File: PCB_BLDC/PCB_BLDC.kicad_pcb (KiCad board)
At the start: 2 copper layers, 152.4 x 119.4 mm, 70 parts, among them J1 Conn_01x01_Female, J10 Conn_01x06, J11 Conn_01x08, J12 Conn_01x06, J13 Conn_01x08, J14 Conn_01x08, J15 Conn_01x10, J16 Conn_01x08, J17 Conn_01x10, J2 Conn_01x01_Female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

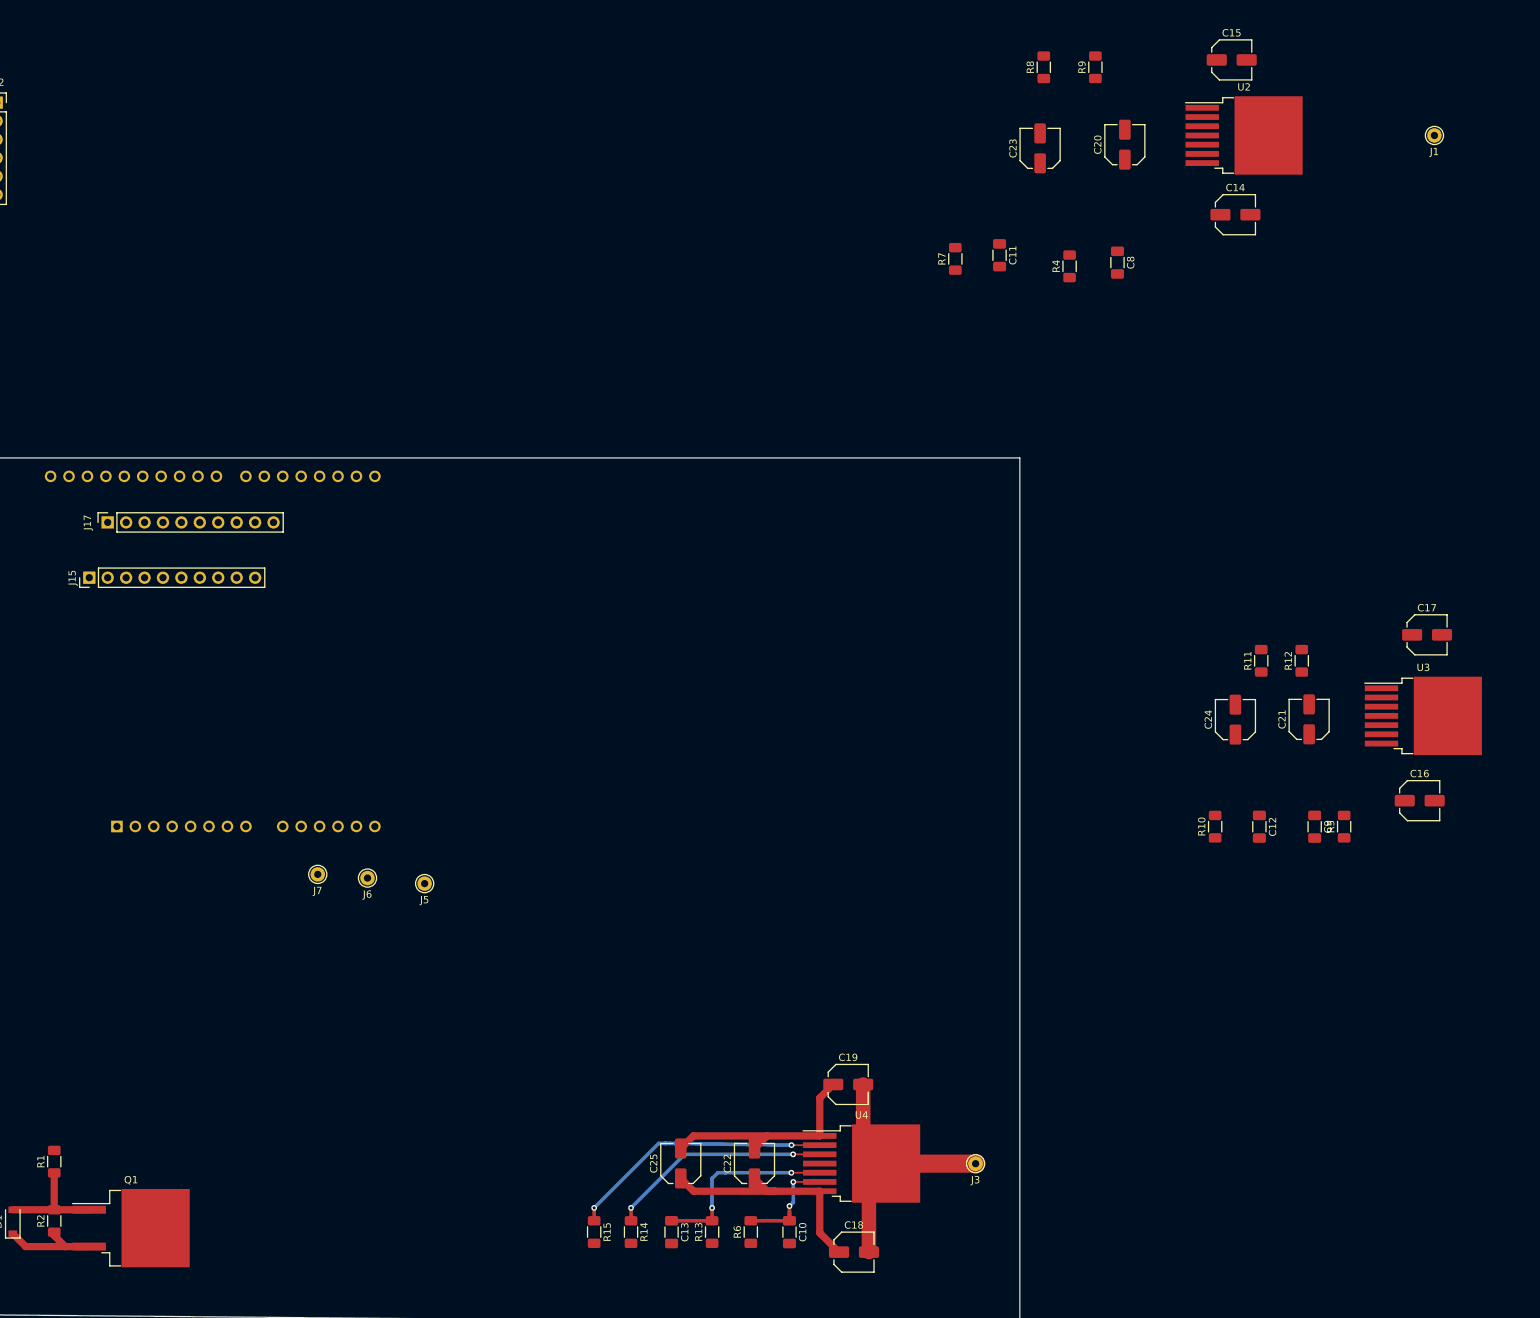
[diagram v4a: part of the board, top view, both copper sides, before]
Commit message: Main: Update Footprint, PCB Layout
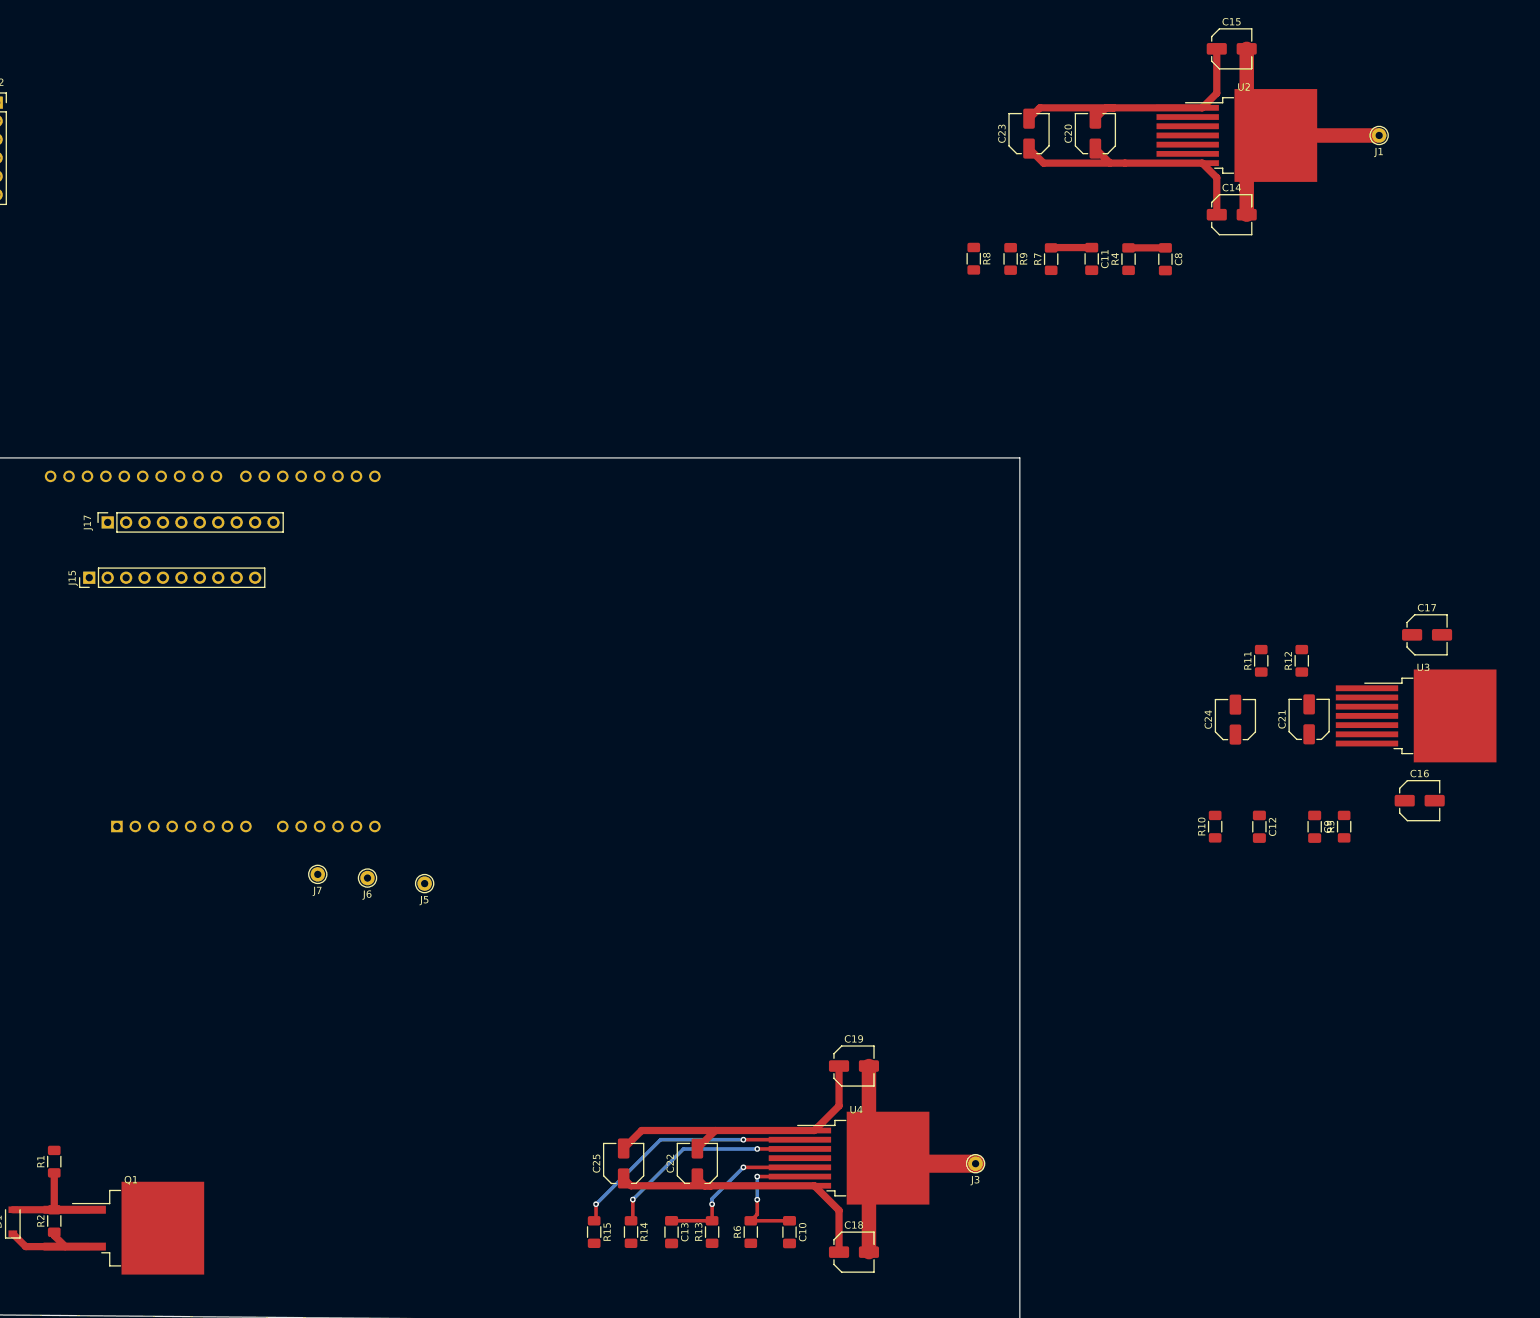
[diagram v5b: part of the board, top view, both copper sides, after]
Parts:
- R3: value 2k -> 100
- moved R9 28.9 mm to (208.3, -68.1), turned to 270 degrees
- moved R8 28.1 mm to (203.2, -68.1), turned to 270 degrees
- moved R7 13.2 mm to (213.9, -68.0)
- moved C11 12.7 mm to (219.5, -68.1)
- moved R4 8.19 mm to (224.5, -68.0)
- moved C22 7.87 mm to (165.1, 56.6)
- moved C25 7.87 mm to (154.9, 56.6)
- moved J1 7.62 mm to (259.1, -85.1)
- moved C8 6.62 mm to (229.6, -68.0)
- moved C20 4.34 mm to (220.0, -85.3)
- moved C19 2.66 mm to (186.7, 43.2)
- moved C23 2.54 mm to (210.8, -85.3)
- moved C15 1.52 mm to (238.8, -97.0)
- moved U4 1.05 mm to (187.0, 55.9)
- moved C14 0.51 mm to (238.8, -74.2)
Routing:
- net GND: track 34.7 -> 82.3 mm
- net /L1_Motor: track 0.00 -> 44.2 mm
- net /VCC_Filtered: track 32.9 -> 75.1 mm
- net /L3_Motor: track 37.7 -> 47.5 mm
- net Net-(C11-Pad1): track 0.00 -> 5.60 mm
- net /L1_IS: track 0.00 -> 5.08 mm
- net /L3_IS: track 15.1 -> 19.7 mm
- net Net-(C13-Pad1): track 27.4 -> 25.3 mm
- net Net-(R15-Pad1): track 36.8 -> 36.2 mm

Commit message: Main: Update Schmeatics, Add VCC
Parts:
- moved C5 216.4 mm to (168.0, 94.4)
- moved C3 172.1 mm to (145.8, 94.4)
- moved J5 149.3 mm to (201.9, 147.4)
- moved J6 149.3 mm to (194.1, 146.7)
- moved J7 149.3 mm to (187.2, 146.2)
- moved C20 143.6 mm to (210.1, 57.9)
- moved C23 143.6 mm to (201.2, 57.9)
- moved C14 143.3 mm to (228.9, 68.8)
- moved C15 143.3 mm to (228.9, 46.0)
- moved J1 143.3 mm to (249.2, 57.9)
- moved U2 143.3 mm to (230.6, 57.9)
- moved C2 138.8 mm to (131.2, 87.2)
- moved A1 136.8 mm to (95.6, 146.6)
- moved C8 120.8 mm to (195.5, 47.8), turned to 90 degrees
- moved L1 120.0 mm to (116.6, 80.5), turned to 0 degrees
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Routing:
- net /VCC_Filtered: track 75.1 -> 309.3 mm
- net /VCC_Polartiy_Check: track 13.5 -> 62.6 mm
- net GND: track 82.3 -> 127.6 mm
- net /L2_IS: track 0.00 -> 41.8 mm, vias 0 -> 2
- net /L2_Motor: track 0.00 -> 41.3 mm
- net /L1_IS: track 5.08 -> 40.4 mm, vias 0 -> 2
- net /VCC_Unregulated: track 0.00 -> 27.1 mm
- net Net-(C12-Pad1): track 0.00 -> 26.4 mm, vias 0 -> 2
- net Net-(C11-Pad1): track 5.60 -> 30.1 mm, vias 0 -> 2
- net /L3_IS: track 19.7 -> 44.1 mm
- net Net-(R15-Pad1): track 36.2 -> 16.5 mm
- net Net-(R9-Pad1): track 0.00 -> 17.5 mm, vias 0 -> 2
- net Net-(R8-Pad1): track 0.00 -> 16.8 mm, vias 0 -> 2
- net Net-(R11-Pad1): track 0.00 -> 16.8 mm, vias 0 -> 2
- net Net-(R12-Pad1): track 0.00 -> 16.5 mm, vias 0 -> 2
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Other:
- board size 152.4 x 119.4 mm -> 242.3 x 147.8 mm

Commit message: Main: Update Arduino Pins, PCB Routing
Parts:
- removed J10: Conn_01x06, Connector_PinHeader_2.54mm:PinHeader_1x06_P2.54mm_Vertical
- removed J11, J14: Conn_01x08, Connector_PinHeader_2.54mm:PinHeader_1x08_P2.54mm_Vertical
- removed J15: Conn_01x10, Connector_PinHeader_2.54mm:PinHeader_1x10_P2.54mm_Vertical
- moved J12 202.5 mm to (92.1, 111.5), turned to 90 degrees
- moved J13 202.0 mm to (69.2, 111.5), turned to 90 degrees
- moved J16 155.3 mm to (87.0, 63.2), turned to 90 degrees
- moved J17 137.3 mm to (60.1, 63.2)
- moved J5 107.6 mm to (188.2, 40.7), turned to 270 degrees
- moved U1 86.4 mm to (83.6, 90.7), turned to 0 degrees
- moved D3 84.3 mm to (68.7, 94.8)
- moved R3 84.3 mm to (75.0, 94.8)
- moved D2 82.3 mm to (103.8, 85.5)
- moved R6 74.9 mm to (135.9, 90.0), turned to 180 degrees
- moved C19 74.8 mm to (166.9, 86.2)
- moved C22 74.8 mm to (145.3, 99.6)
- moved C25 74.8 mm to (135.2, 99.6)
- moved J3 74.8 mm to (183.9, 99.9)
- moved C18 74.8 mm to (166.9, 111.8)
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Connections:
- A1 pad 12: Net-(A1-Pad12) -> /A3
- A1 pad 13: Net-(A1-Pad13) -> /A4
- A1 pad 14: Net-(A1-Pad14) -> /A5
- A1 pad 15: Net-(A1-Pad15) -> /D0
- A1 pad 16: Net-(A1-Pad16) -> /D1
- A1 pad 17: /L1_IN -> /D2
- A1 pad 18: /L2_IN -> /D3
- A1 pad 19: /L3_IN -> /D4
- A1 pad 2: Net-(A1-Pad2) -> /IOREF
- A1 pad 20: /L1_INH -> /D5
- A1 pad 21: /L2_INH -> /D6
- A1 pad 22: /L3_INH -> /D7
- A1 pad 23: /L1_IS -> /D8
- A1 pad 24: /L2_IS -> /D9
- A1 pad 25: /L3_IS -> /D10
- A1 pad 26: Net-(A1-Pad26) -> /D11
- A1 pad 3: Net-(A1-Pad3) -> /Reset
- A1 pad 30: Net-(A1-Pad30) -> /AREF
- A1 pad 31: Net-(A1-Pad31) -> /SDA
- A1 pad 32: Net-(A1-Pad32) -> /SCL
- A1 pad 4: Net-(A1-Pad4) -> /3V3
- A1 pad 5: Net-(A1-Pad5) -> /5V
- C10 pad 1: /L3_IS -> /D3
- C8 pad 1: /L1_IS -> /D7
- C9 pad 1: /L2_IS -> /D5
- J12 pad 1: Net-(J12-Pad1) -> /L1_Sense
- J12 pad 2: Net-(J12-Pad2) -> /L2_Sense
- J12 pad 3: Net-(J12-Pad3) -> /L3_Sense
- J12 pad 4: Net-(J12-Pad4) -> /A3
- J12 pad 5: Net-(J12-Pad5) -> /A4
- J12 pad 6: Net-(J12-Pad6) -> /A5
- J13 pad 2: Net-(J13-Pad2) -> /IOREF
- J13 pad 3: Net-(J13-Pad3) -> /Reset
- J13 pad 4: Net-(J13-Pad4) -> /3V3
- J13 pad 5: Net-(J13-Pad5) -> /5V
- J13 pad 6: Net-(J13-Pad6) -> GND
- J13 pad 7: Net-(J13-Pad7) -> GND
- J13 pad 8: Net-(J13-Pad8) -> /VCC_5V
- J16 pad 1: Net-(J16-Pad1) -> /D7
- J16 pad 2: Net-(J16-Pad2) -> /D6
- J16 pad 3: Net-(J16-Pad3) -> /D5
- J16 pad 4: Net-(J16-Pad4) -> /D4
- J16 pad 5: Net-(J16-Pad5) -> /D3
- J16 pad 6: Net-(J16-Pad6) -> /D2
- J16 pad 7: Net-(J16-Pad7) -> /D1
- J16 pad 8: Net-(J16-Pad8) -> /D0
- J17 pad 1: Net-(J17-Pad1) -> /SCL
- J17 pad 10: Net-(J17-Pad10) -> /D8
- J17 pad 2: Net-(J17-Pad2) -> /SDA
- J17 pad 3: Net-(J17-Pad3) -> /AREF
- J17 pad 4: Net-(J17-Pad4) -> GND
- J17 pad 5: Net-(J17-Pad5) -> /Rot_A_Pull_Up
- J17 pad 6: Net-(J17-Pad6) -> /Rot_B_Pull_Up
- J17 pad 7: Net-(J17-Pad7) -> /D11
- J17 pad 8: Net-(J17-Pad8) -> /D10
- J17 pad 9: Net-(J17-Pad9) -> /D9
- R11 pad 2: /L2_INH -> /D6
- R12 pad 2: /L2_IN -> /D10
- R14 pad 2: /L3_INH -> /D4
- R15 pad 2: /L3_IN -> /D9
- R4 pad 2: /L1_IS -> /D7
- R5 pad 2: /L2_IS -> /D5
- R6 pad 2: /L3_IS -> /D3
- R8 pad 2: /L1_INH -> /D8
- R9 pad 2: /L1_IN -> /D11
- U2 pad 6: /L1_IS -> /D7
- U3 pad 6: /L2_IS -> /D5
- U4 pad 6: /L3_IS -> /D3
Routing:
- net /D11: track 0.00 -> 126.4 mm
- net /D7: track 0.00 -> 118.7 mm, vias 0 -> 2
- net /D3: track 0.00 -> 116.6 mm, vias 0 -> 4
- net /D8: track 0.00 -> 112.8 mm
- net /D10: track 0.00 -> 112.8 mm, vias 0 -> 2
- net /D9: track 0.00 -> 104.6 mm, vias 0 -> 2
- net /D5: track 0.00 -> 101.4 mm, vias 0 -> 4
- net /D4: track 0.00 -> 100.6 mm, vias 0 -> 2
- net /D6: track 0.00 -> 81.8 mm, vias 0 -> 2
- net /L3_IS: track 44.1 -> 0.00 mm, vias 2 -> 0
- net /L2_IS: track 41.8 -> 0.00 mm, vias 2 -> 0
- net /L1_IS: track 40.4 -> 0.00 mm, vias 2 -> 0
- net /VCC_5V: track 15.5 -> 55.2 mm
- net /Rot_B_Pull_Up: track 7.73 -> 37.8 mm
- net /L1_Sense: track 0.00 -> 26.6 mm
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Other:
- board size 242.3 x 147.8 mm -> 268.2 x 169.3 mm

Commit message: Main: Update Routing, Schmematic to use Analog Ports of Arduino
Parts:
- removed J1, J2, J3, J4, J5, J6, J7: Conn_01x01_Female, Connector_Pin:Pin_D1.0mm_L10.0mm
- added J10: Conn_01x06, Connector_PinSocket_2.54mm:PinSocket_1x06_P2.54mm_Vertical, F.Cu at (97.4, 107.8)
- added J11: Conn_01x07, TerminalBlock_Phoenix:TerminalBlock_Phoenix_MKDS-1,5-7_1x07_P5.00mm_Horizontal, F.Cu at (201.9, 95.7)
- moved D2 40.5 mm to (108.5, 125.7)
- moved U1 37.7 mm to (97.5, 125.7), turned to 180 degrees
- moved D3 32.4 mm to (78.9, 125.5)
- moved R3 32.4 mm to (85.2, 125.5)
- moved J9 21.7 mm to (31.5, 123.2)
- moved J8 20.0 mm to (32.0, 143.5)
- moved C12 18.5 mm to (142.7, 74.3)
- moved C1 18.5 mm to (89.8, 147.2)
- moved C10 18.5 mm to (135.9, 103.2)
- moved C11 18.5 mm to (144.2, 41.5)
- moved C13 18.5 mm to (147.9, 106.2)
- moved C14 18.5 mm to (167.4, 62.4)
- moved C15 18.5 mm to (167.4, 39.6)
- moved C16 18.5 mm to (167.1, 95.6)
- moved C17 18.5 mm to (167.1, 71.7)
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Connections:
- net /L1_Sense renamed /A0
- net /L2_Sense renamed /A1
- net /L3_Sense renamed /A2
- C10 pad 1: /D3 -> /L3_IS
- C8 pad 1: /D7 -> /L1_IS
- C9 pad 1: /D5 -> /L2_IS
- R11 pad 2: /D6 -> /D7
- R14 pad 2: /D4 -> /D6
- R4 pad 2: /D7 -> /L1_IS
- R5 pad 2: /D5 -> /L2_IS
- R6 pad 2: /D3 -> /L3_IS
- U2 pad 6: /D7 -> /L1_IS
- U3 pad 6: /D5 -> /L2_IS
- U4 pad 6: /D3 -> /L3_IS
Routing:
- net /L1_Sense: track 0.00 -> 158.8 mm, vias 0 -> 2
- net /L2_Sense: track 0.00 -> 153.4 mm, vias 0 -> 2
- net /L3_Sense: track 0.00 -> 147.8 mm, vias 0 -> 2
- net /L1_IS: track 0.00 -> 124.9 mm, vias 0 -> 2
- net /D3: track 116.6 -> 5.12 mm, vias 4 -> 0
- net /L2_IS: track 0.00 -> 105.3 mm, vias 0 -> 4
- net /VCC_5V: track 55.2 -> 159.8 mm, vias 0 -> 2
- net /D5: track 101.4 -> 5.00 mm, vias 4 -> 0
- net /D4: track 100.6 -> 5.00 mm, vias 2 -> 0
- net /L3_IS: track 0.00 -> 86.6 mm, vias 0 -> 4
- net /L3_Motor: track 47.5 -> 96.8 mm
- net /D7: track 118.7 -> 77.7 mm
- net /L1_Motor: track 44.2 -> 66.3 mm
- net /A0: track 26.6 -> 5.00 mm
- net /L2_Motor: track 41.3 -> 61.9 mm
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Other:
- board size 268.2 x 169.3 mm -> 181.9 x 138.4 mm
